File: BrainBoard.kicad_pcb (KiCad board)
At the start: 4 copper layers, 38.9 x 21.3 mm, 30 parts, among them IC1 STM32G0B1KET6, IC2 MCP2542FDxMF, J2 POWER_IO, J3 COMMS, J4 CAN, U7 TPS62162DSG

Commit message: Changed CAN port to 3pin;
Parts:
- removed J4: CAN, Connector_JST:JST_GH_BM02B-GHS-TBT_1x02-1MP_P1.25mm_Vertical
- added J5: CAN, Connector_JST:JST_GH_BM03B-GHS-TBT_1x03-1MP_P1.25mm_Vertical, F.Cu at (131.8, 77.2)
- moved C4 1.05 mm to (126.6, 79.4), turned to 90 degrees
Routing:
- net /I2C_SDA: track 25.4 -> 21.7 mm
- net /CAN+: track 22.5 -> 21.8 mm
- net /CAN-: track 25.4 -> 24.9 mm
- net /ADC_2: track 22.0 -> 21.5 mm
- net /ADC_3: track 13.3 -> 12.8 mm
- net GND: vias 7 -> 9

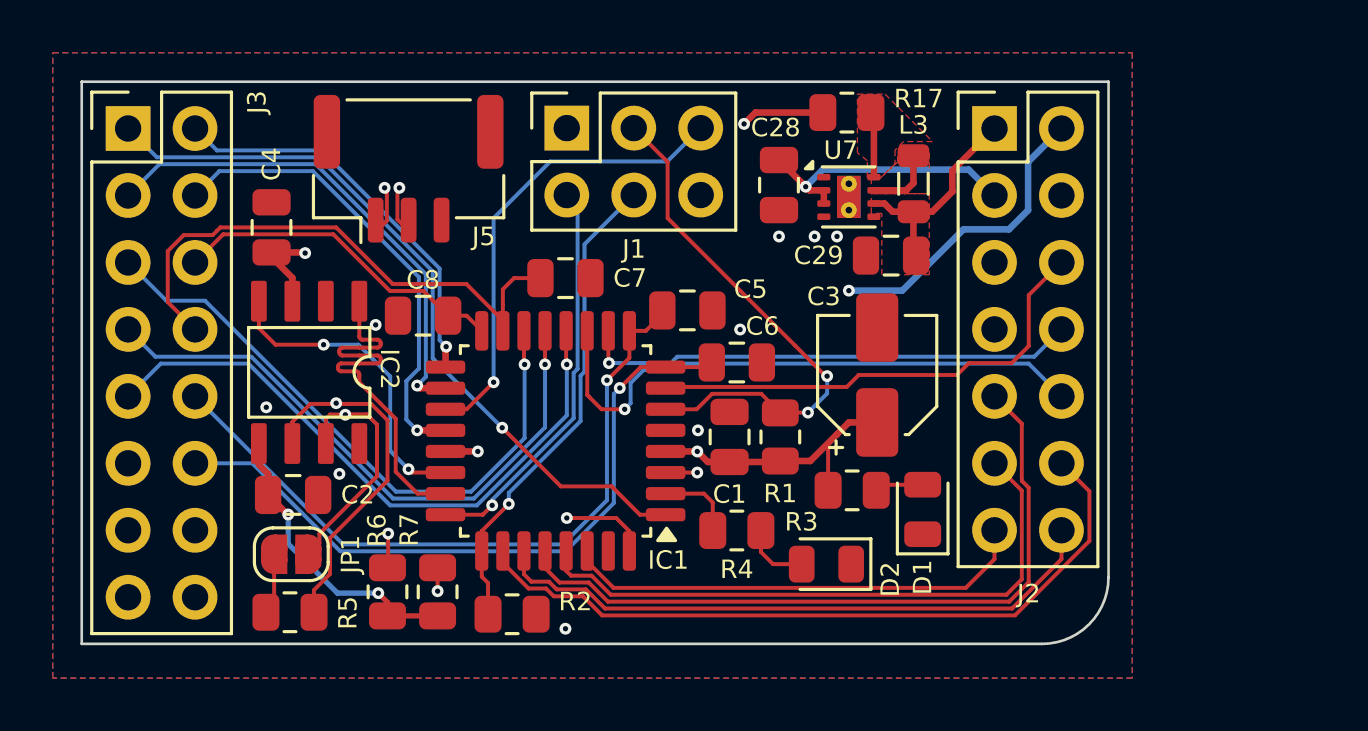
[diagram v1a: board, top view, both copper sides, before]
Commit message: Schematic overhaul: Added separated sheets for functions, Added 5V DCDC, Board overhaul: Modified to be MFR ready, Added 5V DCDC,
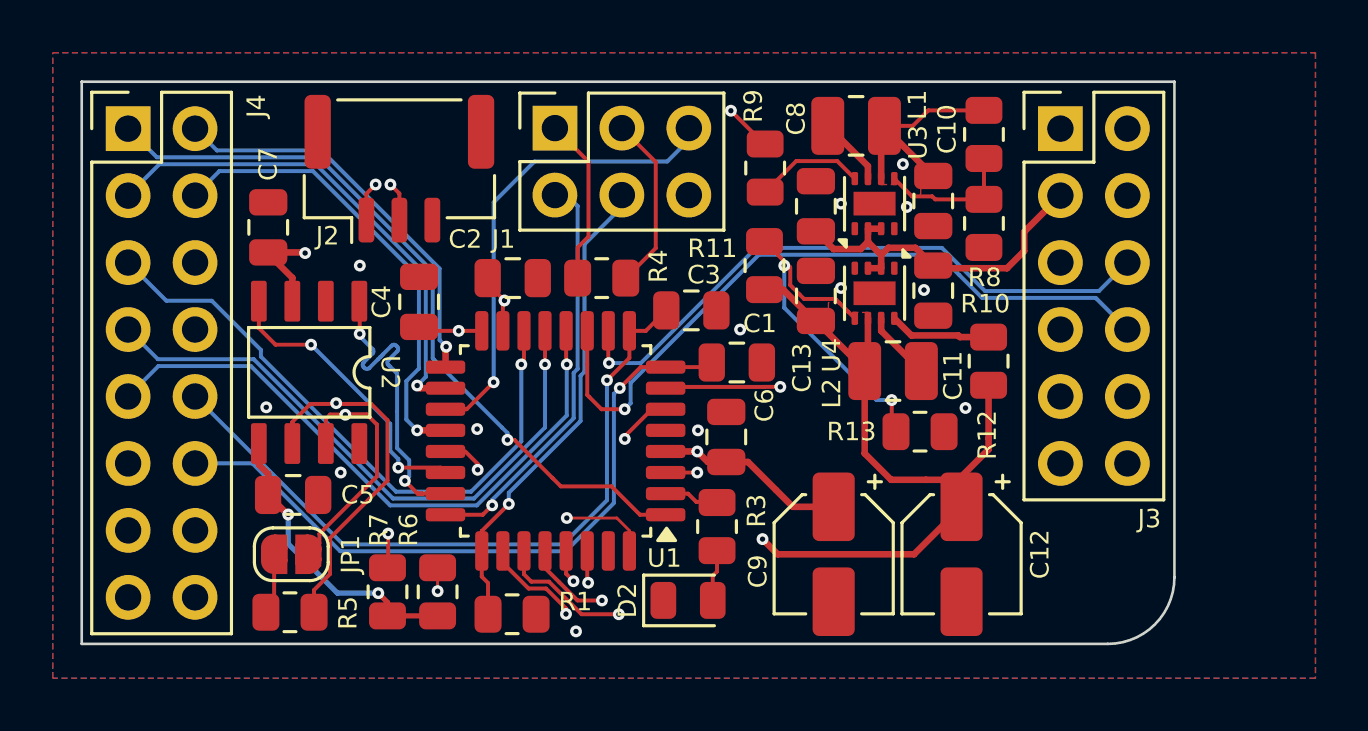
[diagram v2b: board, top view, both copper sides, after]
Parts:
- removed C28, C29: 1uF, Capacitor_SMD:C_0805_2012Metric
- removed the C3 at (149.6, 85.0)
- removed D1: KP-2012LSGC, LED_SMD:LED_0805_2012Metric
- removed IC1: STM32G0B1KET6, Package_QFP:LQFP-32_7x7mm_P0.8mm
- removed IC2: MCP2542FDxMF, Package_SO:SOIC-8_NO_PAD
- removed J5: CAN, Connector_JST:JST_GH_BM03B-GHS-TBT_1x03-1MP_P1.25mm_Vertical
- removed L3: MLZ2012A2R2WT000, Inductor_SMD:L_0805_2012Metric
- removed R17: 100kΩ, Resistor_SMD:R_0805_2012Metric
- removed the R3 at (148.6, 89.4)
- removed U7: TPS62162DSG, Package_SON:WSON-8-1EP_2x2mm_P0.5mm_EP0.9x1.6mm_ThermalVias
- added C10: 1uF, Capacitor_SMD:C_0805_2012Metric, F.Cu at (151.7, 78.4)
- added C11: 1uF, Capacitor_SMD:C_0805_2012Metric, F.Cu at (151.7, 81.8)
- added C12: 10uF, Capacitor_SMD:CP_Elec_4x5.4, F.Cu at (152.8, 91.8)
- added C13: 1uF, Capacitor_SMD:C_0805_2012Metric, F.Cu at (147.2, 82.0)
- added C8: 1uF, Capacitor_SMD:C_0805_2012Metric, F.Cu at (147.2, 78.6)
- added C9: 10uF, Capacitor_SMD:CP_Elec_4x5.4, F.Cu at (147.9, 91.8)
- added J4: COMMS, Connector_PinHeader_2.54mm:PinHeader_2x08_P2.54mm_Vertical, F.Cu at (121.1, 75.7)
- added L1: LQM2HPN2R2MJ0L, Inductor_SMD:L_1008_2520Metric, F.Cu at (148.8, 75.5)
- added L2: LQM2HPN2R2MJ0L, Inductor_SMD:L_1008_2520Metric, F.Cu at (150.2, 84.8)
- added R10: 100kΩ, Resistor_SMD:R_0805_2012Metric, F.Cu at (153.6, 79.2)
- added R11: 52.5kΩ, Resistor_SMD:R_0805_2012Metric, F.Cu at (145.3, 80.8)
- added R12: 100kΩ, Resistor_SMD:R_0805_2012Metric, F.Cu at (153.8, 84.5)
- added R13: 100kΩ, Resistor_SMD:R_0805_2012Metric, F.Cu at (151.2, 87.2)
- added R8: 31.6kΩ, Resistor_SMD:R_0805_2012Metric, F.Cu at (153.6, 75.9)
- added R9: 100kΩ, Resistor_SMD:R_0805_2012Metric, F.Cu at (145.3, 77.2)
- added U1: STM32G0B1KET6, Package_QFP:LQFP-32_7x7mm_P0.8mm, F.Cu at (137.3, 87.5)
- added U2: MCP2542FDxMF, Package_SO:SOIC-8_NO_PAD, F.Cu at (130.7, 84.9)
- added U3: TPS62170DSG, Package_SON:WSON-8-1EP_2x2mm_P0.5mm_EP0.9x1.6mm, F.Cu at (149.4, 78.5)
- added U4: TPS62170DSG, Package_SON:WSON-8-1EP_2x2mm_P0.5mm_EP0.9x1.6mm, F.Cu at (149.4, 81.9)
- J2: value POWER_IO -> CAN; footprint Connector_PinHeader_2.54mm:PinHeader_2x07_P2.54mm_Vertical -> Connector_JST:JST_GH_BM03B-GHS-TBT_1x03-1MP_P1.25mm_Vertical
- J3: value COMMS -> POWER_IO; footprint Connector_PinHeader_2.54mm:PinHeader_2x08_P2.54mm_Vertical -> Connector_PinHeader_2.54mm:PinHeader_2x06_P2.54mm_Vertical
- moved J3 35.4 mm to (156.5, 75.7)
- moved J2 22.6 mm to (131.4, 77.2)
- moved R4 9.07 mm to (139.1, 81.3), turned to 180 degrees
- moved D2 5.43 mm to (142.4, 93.5), turned to 0 degrees
- moved C2 2.00 mm to (135.7, 81.3)
- moved R6 1.90 mm to (132.9, 93.2), turned to 90 degrees
- moved R7 1.90 mm to (131.0, 93.2), turned to -90 degrees
- moved R3 0.76 mm to (143.5, 90.8), turned to 90 degrees
- moved C4 0.55 mm to (132.2, 82.2), turned to 90 degrees
- moved J1 0.45 mm to (137.3, 75.6)
- moved C3 0.15 mm to (142.5, 82.5)
- moved C6 0.12 mm to (143.8, 87.3)
- moved C7 0.12 mm to (126.5, 79.4)
- renumbered C6 to C1, C7 to C2, C5 to C3, C8 to C4, C2 to C5, C1 to C6, C4 to C7, R2 to R1, R4 to R3, R1 to R4
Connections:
- net /SW_CLK renamed /MCU/SW_CLK
- net /SW_RST renamed /MCU/SW_RST
- C1 pad 1: /ADC_0 -> /ADC0
- C2 pad 1: /ADC_2 -> /ADC2
- C3 pad 1: /ADC_1 -> /ADC1
- C4 pad 1: /ADC_3 -> /ADC3
- J1 pad 2: /SW_DIO -> /MCU/SW_DIO
- J1 pad 5: /SW_TX -> /MCU/SW_TX
- J2 pad 1: 3.3V -> /CAN/CAN-
- J2 pad 2: 5V -> /CAN/CAN+
- J2 pad 3: 12V -> GND
- J3 pad 1: /UART_RX -> 3.3V
- J3 pad 10: /ADC_1 -> /BOARD_TYPE4
- J3 pad 11: GND -> /BOARD_TYPE0
- J3 pad 12: /ADC_0 -> /BOARD_TYPE3
- J3 pad 2: /UART_TX -> GND
- J3 pad 3: /PWM_11 -> 12V
- J3 pad 4: /PWM_31 -> /SPI_SS0
- J3 pad 5: /SPI_MOSI -> /SPI_SS3
- J3 pad 6: /ADC_3 -> /SPI_SS1
- J3 pad 7: /SPI_MISO -> /BOARD_TYPE2
- J3 pad 8: /ADC_2 -> /SPI_SS2
- J3 pad 9: /SPI_SCK -> /BOARD_TYPE1
- JP1 pad 2: /CAN+ -> /CAN/CAN+
- R3 pad 2: /USER -> /MCU/USER
- R5 pad 1: /CAN- -> /CAN/CAN-
- R6 pad 1: /I2C_SDA -> 3.3V
- R6 pad 2: 3.3V -> /I2C_SCL
- R7 pad 1: 3.3V -> /I2C_SDA
- R7 pad 2: /I2C_SCL -> 3.3V
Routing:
- net /BOARD_TYPE2: track 0.00 -> 32.4 mm, vias 0 -> 1
- net /BOARD_TYPE4: track 0.00 -> 31.7 mm, vias 0 -> 1
- net /BOARD_TYPE3: track 0.00 -> 28.7 mm, vias 0 -> 1
- net /BOARD_TYPE1: track 0.00 -> 28.4 mm, vias 0 -> 1
- net /BOARD_TYPE_4: track 28.1 -> 0.00 mm
- net /BOARD_TYPE_2: track 27.4 -> 0.00 mm
- net 5V: track 36.6 -> 63.7 mm
- net /ADC_1: track 27.0 -> 0.00 mm, vias 1 -> 0
- net /ADC1: track 0.00 -> 27.0 mm, vias 0 -> 1
- net /ADC_0: track 26.3 -> 0.00 mm, vias 1 -> 0
- net /ADC0: track 0.00 -> 26.3 mm, vias 0 -> 1
- net /CAN-: track 24.9 -> 0.00 mm, vias 2 -> 0
- net /CAN/CAN-: track 0.00 -> 24.5 mm, vias 0 -> 2
- net /BOARD_TYPE0: track 0.00 -> 24.2 mm, vias 0 -> 1
- net /BOARD_TYPE_3: track 23.7 -> 0.00 mm
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- added copper zone on F.Cu, net 5V
- removed copper zone on F.Cu, net Net-(U7-PG)
- removed copper zone on F.Cu, net Net-(U7-SW)
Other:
- board size 38.9 x 21.3 mm -> 41.4 x 21.3 mm
